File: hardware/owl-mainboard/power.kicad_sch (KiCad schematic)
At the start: 45 parts, among them J101 Battery +, -, U101 BQ24073RGTR, U102 MAX17048G+T10, U103 TPS63802DLAR, U104 TPS22917DBVR

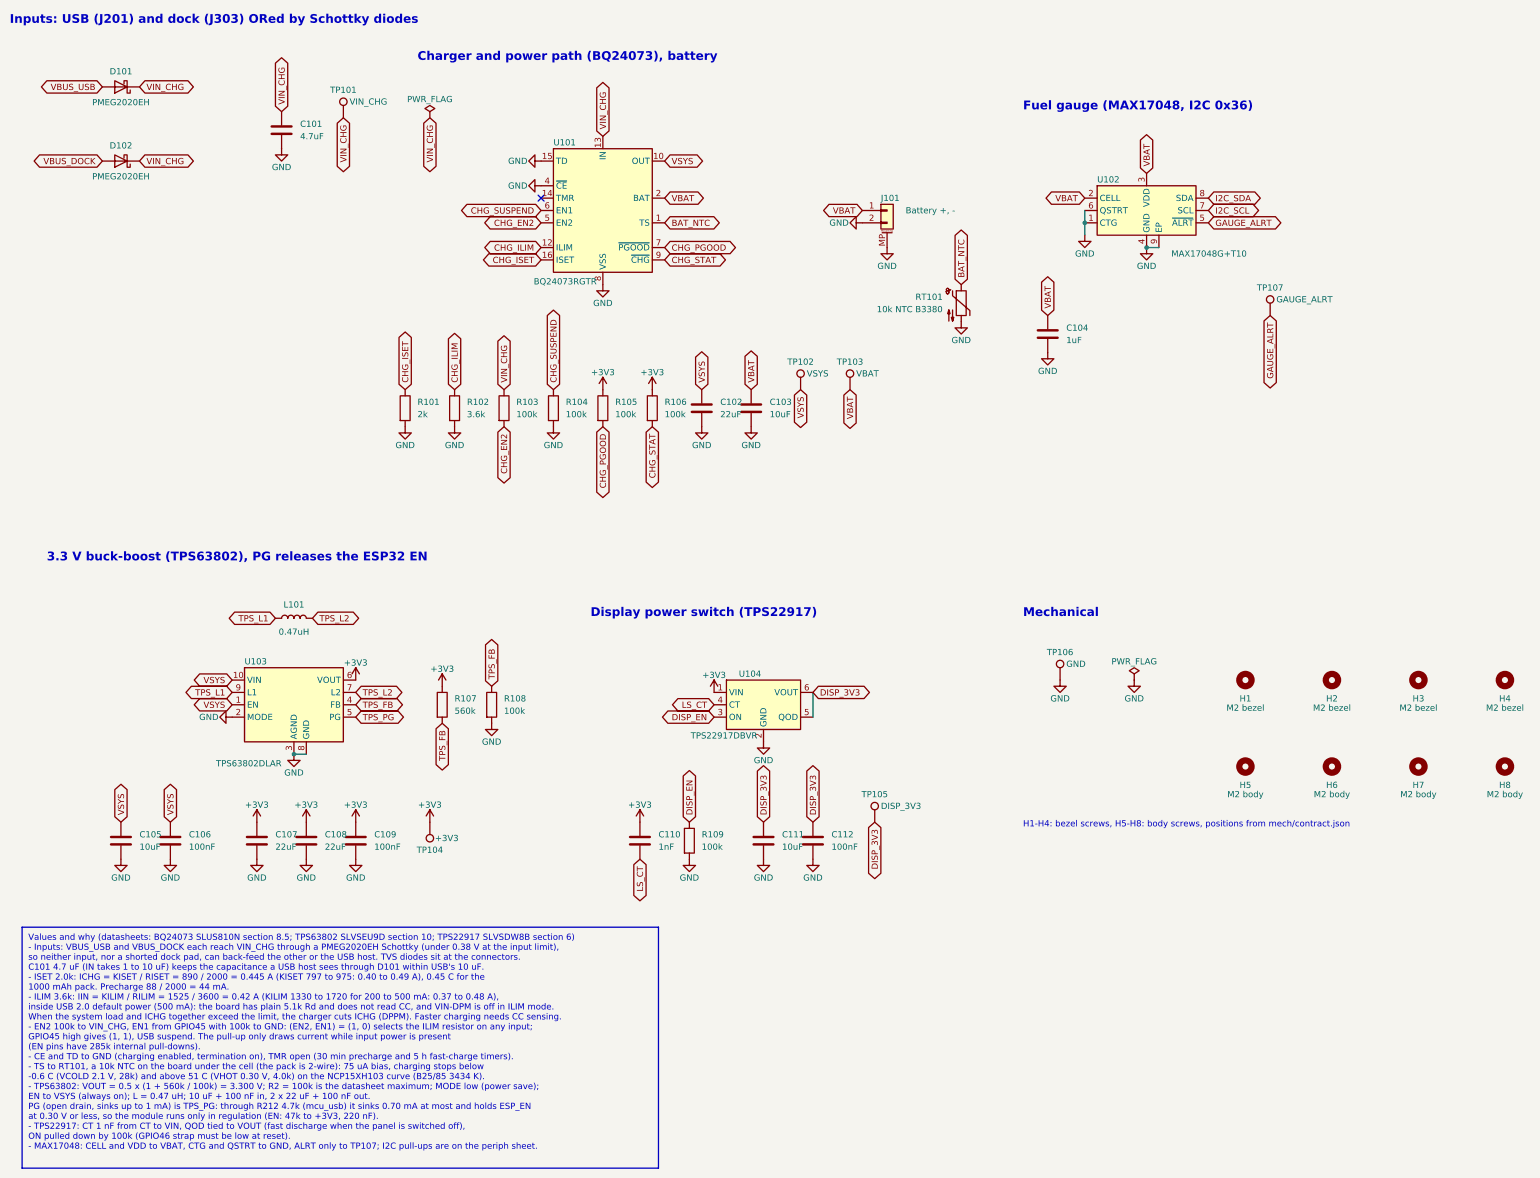
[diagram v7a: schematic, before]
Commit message: feat(hardware): make RT101 a B25/50 3950 K NTC and recompute the TS cut-offs
Controller ruling: RT101 becomes Sunlord SDNT1005X103F3950FTF (C95939, 10k, 1 % on R25 and on
B, B25/50 3950 K, 0402, JLC Extended, stock 184396; no Basic or Preferred 10k NTC exists). The
alternate is KUU KNTC0402/10KF3950 (C41366926), also 3950 K at 1 %. Height 0.65 mm (0.5 +- 0.15).

The steeper curve narrows the BQ24073 charge window from the 103AT-2's 0 to 50 C to 47.2 C hot
(release 44.7 C, worst case 43.2 to 51.5 C) and +3.5 C cold (release 6.5 C, worst case +1.4 to
+5.6 C), from VHOT, VCOLD and INTC in SLUS810N 8.5 and RT101's own tolerances. rev-a.md,
bringup.md, design.toml and the power sheet note carry the new numbers; rev-a.md adds that
charging may pause in a warm room. Also fixes the review's M2 nits (-0.6 C on the NCP15XH103,
a 0.45 A charge).
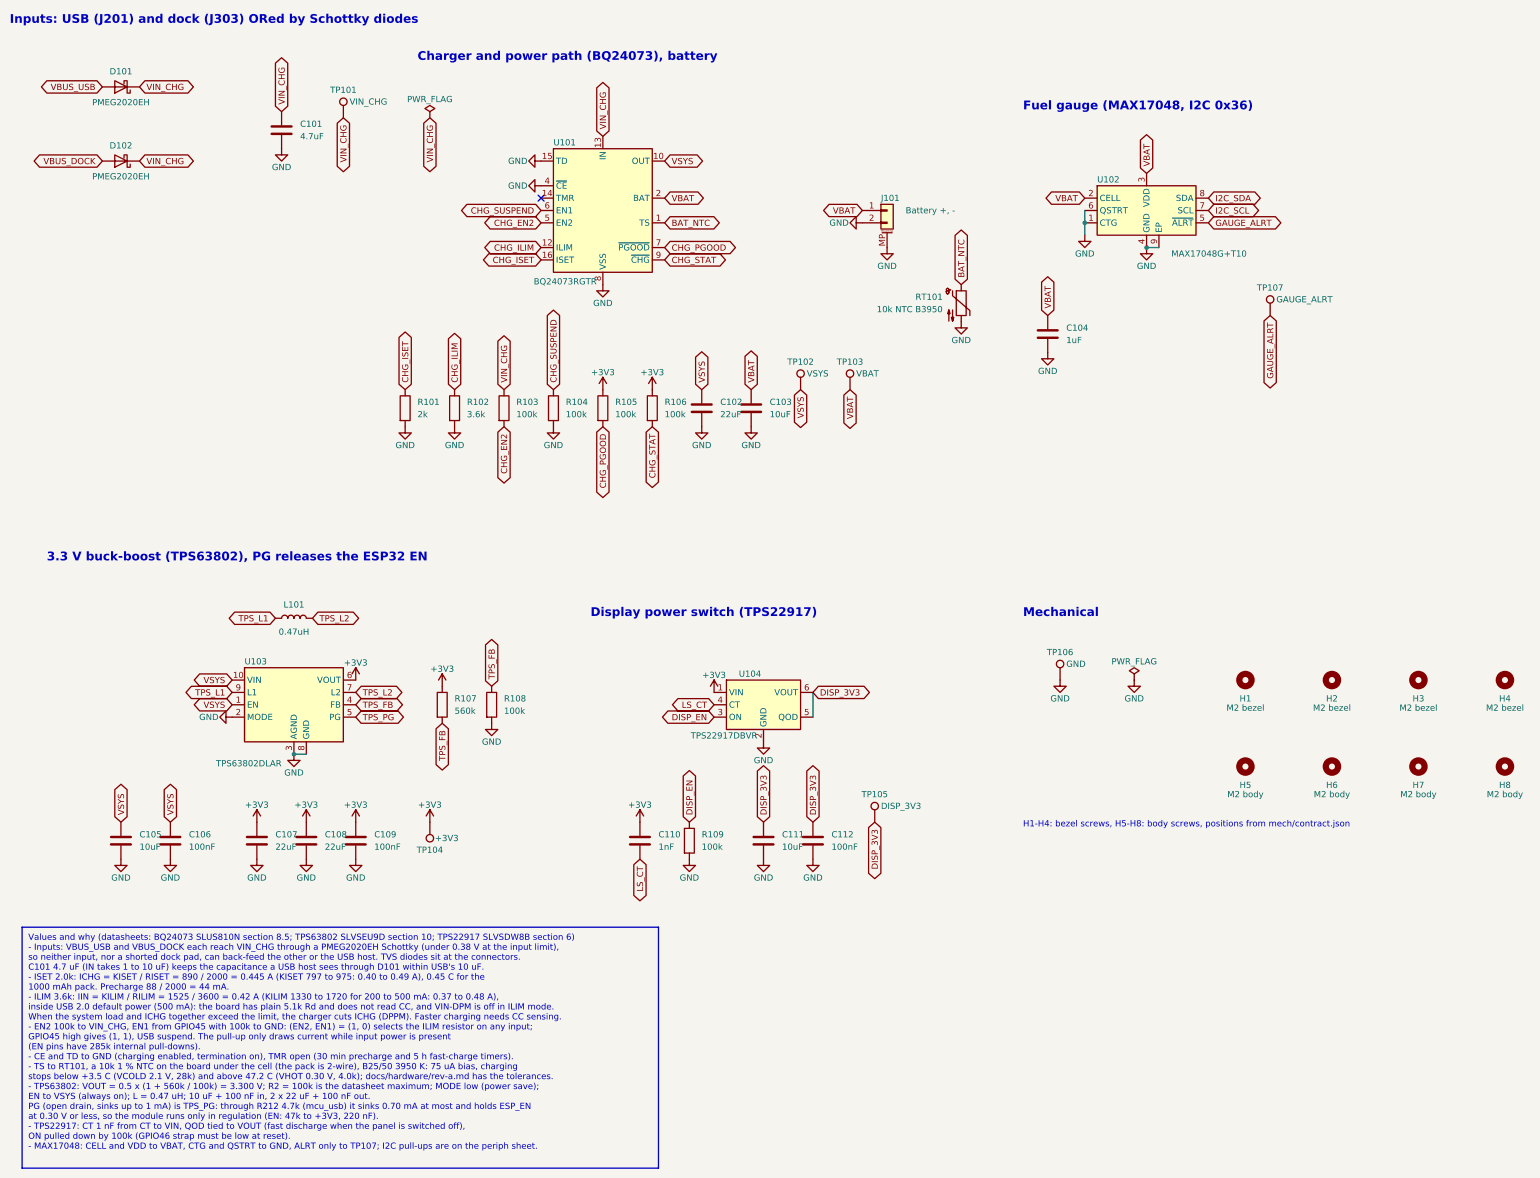
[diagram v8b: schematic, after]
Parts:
- RT101: value 10k NTC B3380 -> 10k NTC B3950; LCSC Part # C77131 -> C95939; MPN NCP15XH103F03RC -> SDNT1005X103F3950FTF; Manufacturer Murata Electronics -> Sunlord
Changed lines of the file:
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@@
 		)
 	)
-	(text_box "Values and why (datasheets: BQ24073 SLUS810N section 8.5; TPS63802 SLVSEU9D section 10; TPS22917 SLVSDW8B section 6)\n- Inputs: VBUS_USB and VBUS_DOCK each reach VIN_CHG through a PMEG2020EH Schottky (under 0.38 V at the input limit),\n  so neither input, nor a shorted dock pad, can back-feed the other or the USB host. TVS diodes sit at the connectors.\n  C101 4.7 uF (IN takes 1 to 10 uF) keeps the capacitance a USB host sees through D101 within USB's 10 uF.\n- ISET 2.0k: ICHG = KISET / RISET = 890 / 2000 = 0.445 A (KISET 797 to 975: 0.40 to 0.49 A), 0.45 C for the\n  1000 mAh pack. Precharge 88 / 2000 = 44 mA.\n- ILIM 3.6k: IIN = KILIM / RILIM = 1525 / 3600 = 0.42 A (KILIM 1330 to 1720 for 200 to 500 mA: 0.37 to 0.48 A),\n  inside USB 2.0 default power (500 mA): the board has plain 5.1k Rd and does not read CC, and VIN-DPM is off in ILIM mode.\n  When the system load and ICHG together exceed the limit, the charger cuts ICHG (DPPM). Faster charging needs CC sensing.\n- EN2 100k to VIN_CHG, EN1 from GPIO45 with 100k to GND: (EN2, EN1) = (1, 0) selects the ILIM resistor on any input;\n  GPIO45 high gives (1, 1), USB suspend. The pull-up only draws current while input power is present\n  (EN pins have 285k internal pull-downs).\n- CE and TD to GND (charging enabled, termination on), TMR open (30 min precharge and 5 h fast-charge timers).\n- TS to RT101, a 10k NTC on the board under the cell (the pack is 2-wire): 75 uA bias, charging stops below\n  -0.6 C (VCOLD 2.1 V, 28k) and above 51 C (VHOT 0.30 V, 4.0k) on the NCP15XH103 curve (B25/85 3434 K).\n- TPS63802: VOUT = 0.5 x (1 + 560k / 100k) = 3.300 V; R2 = 100k is the datasheet maximum; MODE low (power save);\n  EN to VSYS (always on); L = 0.47 uH; 10 uF + 100 nF in, 2 x 22 uF + 100 nF out.\n  PG (open drain, sinks up to 1 mA) is TPS_PG: through R212 4.7k (mcu_usb) it sinks 0.70 mA at most and holds ESP_EN\n  at 0.30 V or less, so the module runs only in regulation (EN: 47k to +3V3, 220 nF).\n- TPS22917: CT 1 nF from CT to VIN, QOD tied to VOUT (fast discharge when the panel is switched off),\n  ON pulled down by 100k (GPIO46 strap must be low at reset).\n- MAX17048: CELL and VDD to VBAT, CTG and QSTRT to GND, ALRT only to TP107; I2C pull-ups are on the periph sheet."
+	(text_box "Values and why (datasheets: BQ24073 SLUS810N section 8.5; TPS63802 SLVSEU9D section 10; TPS22917 SLVSDW8B section 6)\n- Inputs: VBUS_USB and VBUS_DOCK each reach VIN_CHG through a PMEG2020EH Schottky (under 0.38 V at the input limit),\n  so neither input, nor a shorted dock pad, can back-feed the other or the USB host. TVS diodes sit at the connectors.\n  C101 4.7 uF (IN takes 1 to 10 uF) keeps the capacitance a USB host sees through D101 within USB's 10 uF.\n- ISET 2.0k: ICHG = KISET / RISET = 890 / 2000 = 0.445 A (KISET 797 to 975: 0.40 to 0.49 A), 0.45 C for the\n  1000 mAh pack. Precharge 88 / 2000 = 44 mA.\n- ILIM 3.6k: IIN = KILIM / RILIM = 1525 / 3600 = 0.42 A (KILIM 1330 to 1720 for 200 to 500 mA: 0.37 to 0.48 A),\n  inside USB 2.0 default power (500 mA): the board has plain 5.1k Rd and does not read CC, and VIN-DPM is off in ILIM mode.\n  When the system load and ICHG together exceed the limit, the charger cuts ICHG (DPPM). Faster charging needs CC sensing.\n- EN2 100k to VIN_CHG, EN1 from GPIO45 with 100k to GND: (EN2, EN1) = (1, 0) selects the ILIM resistor on any input;\n  GPIO45 high gives (1, 1), USB suspend. The pull-up only draws current while input power is present\n  (EN pins have 285k internal pull-downs).\n- CE and TD to GND (charging enabled, termination on), TMR open (30 min precharge and 5 h fast-charge timers).\n- TS to RT101, a 10k 1 % NTC on the board under the cell (the pack is 2-wire), B25/50 3950 K: 75 uA bias, charging\n  stops below +3.5 C (VCOLD 2.1 V, 28k) and above 47.2 C (VHOT 0.30 V, 4.0k); docs/hardware/rev-a.md has the tolerances.\n- TPS63802: VOUT = 0.5 x (1 + 560k / 100k) = 3.300 V; R2 = 100k is the datasheet maximum; MODE low (power save);\n  EN to VSYS (always on); L = 0.47 uH; 10 uF + 100 nF in, 2 x 22 uF + 100 nF out.\n  PG (open drain, sinks up to 1 mA) is TPS_PG: through R212 4.7k (mcu_usb) it sinks 0.70 mA at most and holds ESP_EN\n  at 0.30 V or less, so the module runs only in regulation (EN: 47k to +3V3, 220 nF).\n- TPS22917: CT 1 nF from CT to VIN, QOD tied to VOUT (fast discharge when the panel is switched off),\n  ON pulled down by 100k (GPIO46 strap must be low at reset).\n- MAX17048: CELL and VDD to VBAT, CTG and QSTRT to GND, ALRT only to TP107; I2C pull-ups are on the periph sheet."
 		(exclude_from_sim no)
 		(at 20.32 223.52 0)
@@
 			)
 		)
-		(property "Value" "10k NTC B3380"
+		(property "Value" "10k NTC B3950"
 			(at 209.55 96.52 0)
 			(show_name no)
@@
 			)
 		)
-		(property "LCSC Part #" "C77131"
+		(property "LCSC Part #" "C95939"
 			(at 213.36 95.25 0)
 			(hide yes)
@@
 			)
 		)
-		(property "MPN" "NCP15XH103F03RC"
+		(property "MPN" "SDNT1005X103F3950FTF"
 			(at 213.36 95.25 0)
 			(hide yes)
@@
 			)
 		)
-		(property "Manufacturer" "Murata Electronics"
+		(property "Manufacturer" "Sunlord"
 			(at 213.36 95.25 0)
 			(hide yes)
